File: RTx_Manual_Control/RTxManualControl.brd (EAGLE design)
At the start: 58.4 x 49 mm, 36 parts

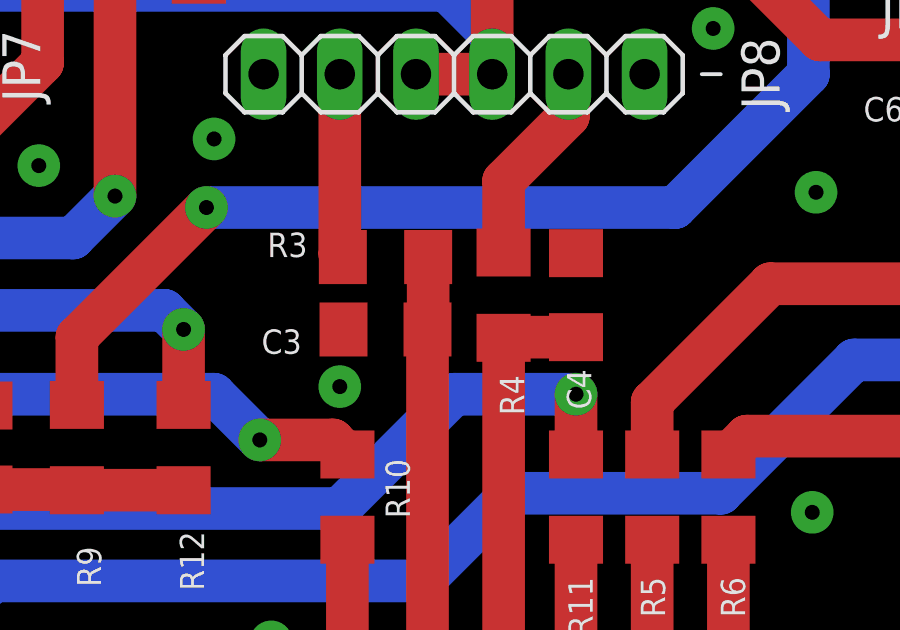
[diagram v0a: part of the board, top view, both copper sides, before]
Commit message: Added values for manual input LPF components. Completed RTx Manual Remote Design document.
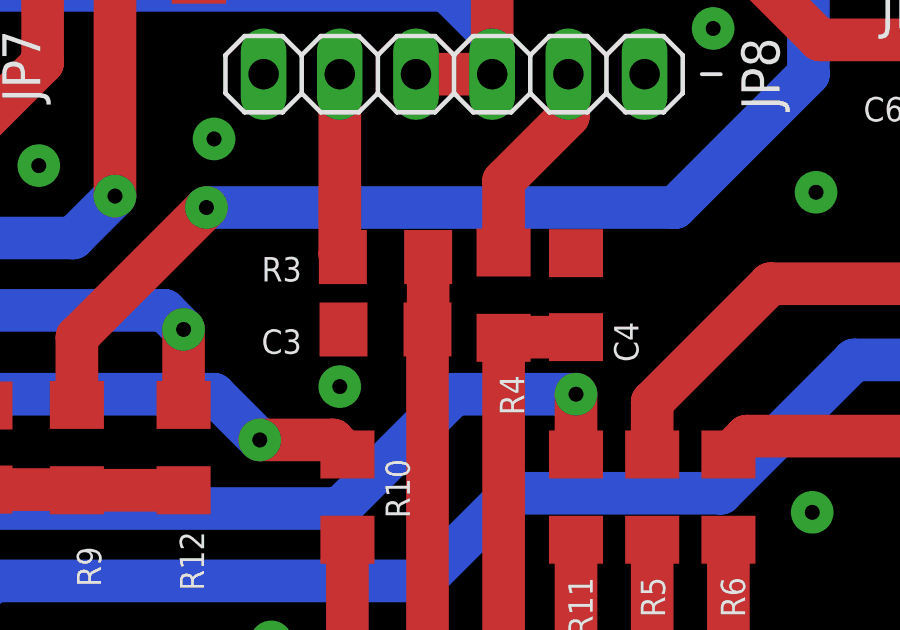
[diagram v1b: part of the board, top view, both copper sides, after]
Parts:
- C1, C2, C3, C4: value (none) -> 10u
- R1, R2, R3, R4: value (none) -> 620
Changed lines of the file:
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@@
 </autorouter>
 <elements>
-<element name="C1" library="rcl" package="C1206" value="" x="6.223" y="39.751" smashed="yes" rot="R270">
+<element name="C1" library="rcl" package="C1206" value="10u" x="6.223" y="39.751" smashed="yes" rot="R270">
 <attribute name="NAME" x="6.985" y="43.18" size="0.8128" layer="25" rot="R180"/>
-<attribute name="VALUE" x="3.683" y="41.021" size="1.27" layer="27" rot="R270"/>
 </element>
-<element name="C2" library="rcl" package="C1206" value="" x="13.716" y="39.751" smashed="yes" rot="R270">
+<element name="C2" library="rcl" package="C1206" value="10u" x="13.716" y="39.751" smashed="yes" rot="R270">
 <attribute name="NAME" x="14.478" y="43.18" size="0.8128" layer="25" rot="R180"/>
-<attribute name="VALUE" x="11.176" y="41.021" size="1.27" layer="27" rot="R270"/>
 </element>
-<element name="C3" library="rcl" package="C1206" value="" x="32.893" y="14.859" smashed="yes" rot="R180">
+<element name="C3" library="rcl" package="C1206" value="10u" x="32.893" y="14.859" smashed="yes" rot="R180">
 <attribute name="NAME" x="30.099" y="14.859" size="0.8128" layer="25" rot="R180"/>
-<attribute name="VALUE" x="34.163" y="17.399" size="1.27" layer="27" rot="R180"/>
 </element>
-<element name="C4" library="rcl" package="C1206" value="" x="39.243" y="16.002" smashed="yes" rot="R90">
-<attribute name="NAME" x="39.751" y="12.192" size="0.8128" layer="25" rot="R90"/>
-<attribute name="VALUE" x="41.783" y="14.732" size="1.27" layer="27" rot="R90"/>
+<element name="C4" library="rcl" package="C1206" value="10u" x="39.243" y="16.002" smashed="yes" rot="R90">
+<attribute name="NAME" x="40.513" y="15.113" size="0.8128" layer="25" rot="R270"/>
 </element>
-<element name="R1" library="rcl" package="R1206" value="" x="8.89" y="39.751" smashed="yes" rot="R90">
+<element name="R1" library="rcl" package="R1206" value="620" x="8.89" y="39.751" smashed="yes" rot="R90">
 <attribute name="NAME" x="9.652" y="43.18" size="0.8128" layer="25" rot="R180"/>
-<attribute name="VALUE" x="11.43" y="38.481" size="1.27" layer="27" rot="R90"/>
 </element>
-<element name="R2" library="rcl" package="R1206" value="" x="16.383" y="39.751" smashed="yes" rot="R90">
+<element name="R2" library="rcl" package="R1206" value="620" x="16.383" y="39.751" smashed="yes" rot="R90">
 <attribute name="NAME" x="17.145" y="43.18" size="0.8128" layer="25" rot="R180"/>
-<attribute name="VALUE" x="18.923" y="38.481" size="1.27" layer="27" rot="R90"/>
 </element>
-<element name="R3" library="rcl" package="R1206" value="" x="32.893" y="17.272" smashed="yes">
-<attribute name="NAME" x="28.956" y="17.272" size="0.8128" layer="25"/>
-<attribute name="VALUE" x="31.623" y="14.732" size="1.27" layer="27"/>
+<element name="R3" library="rcl" package="R1206" value="620" x="32.893" y="17.272" smashed="yes">
+<attribute name="NAME" x="30.099" y="17.272" size="0.8128" layer="25" rot="R180"/>
 </element>
-<element name="R4" library="rcl" package="R1206" value="" x="36.83" y="16.002" smashed="yes" rot="R270">
+<element name="R4" library="rcl" package="R1206" value="620" x="36.83" y="16.002" smashed="yes" rot="R270">
 <attribute name="NAME" x="36.703" y="13.335" size="0.8128" layer="25" rot="R270"/>
-<attribute name="VALUE" x="34.29" y="17.272" size="1.27" layer="27" rot="R270"/>
 </element>
 <element name="JP3" library="pinhead" package="1X03" value="Neutral LEDs" x="52.07" y="13.843" smashed="yes" rot="R270">
@@
 <element name="R11" library="rcl" package="R1206" value="280" x="39.243" y="9.271" smashed="yes" rot="R270">
 <attribute name="NAME" x="38.989" y="6.604" size="0.8128" layer="25" rot="R270"/>
-<attribute name="VALUE" x="36.703" y="10.541" size="1.27" layer="27" rot="R270"/>
 </element>
 <element name="R12" library="rcl" package="R1206" value="1k" x="26.162" y="10.922" smashed="yes" rot="R270">
